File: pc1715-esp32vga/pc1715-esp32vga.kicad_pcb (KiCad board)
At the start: 2 copper layers, 110 x 38 mm, 31 parts, among them J1001 IDC10_VIDEO_IN, J1002 VGAOUT, J1003 USB_B, J1004 KEYPAD, J1005 IDC16_VGAOUT, SW1001 RST, U1001 ESP32-S3-WROOM-1, U1002 LM1117MP-3.3

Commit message: IDC10 Beschriftung
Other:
- board text added: "10 8 6 4 2"
- board text added: "10 BSYNC 6 INTENS 4 VIDEO 1,2 +5V 3 +3,3V 5,7,8,9 GND"
- board text added: "9 7 5 3 1"
- board text removed: "10 BSYNC 6 INTENS 4 VIDEO 1,2 +5V 3,5,7,8,9 GND"
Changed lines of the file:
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@@
 		(layer "Edge.Cuts")
+	)
+	(gr_text "10 8 6 4 2"
+		(at 162.56 76.708 0)
+		(layer "B.SilkS")
+		(effects
+			(font
+				(size 1.25 1.25)
+				(thickness 0.25)
+				(bold yes)
+			)
+			(justify left bottom mirror)
+		)
+	)
+	(gr_text "9 7  5  3 1"
+		(at 162.56 84.582 0)
+		(layer "B.SilkS")
+		(effects
+			(font
+				(size 1.25 1.25)
+				(thickness 0.25)
+				(bold yes)
+			)
+			(justify left bottom mirror)
+		)
 	)
 	(gr_text "Robotron VGA Adapter\nDesign (c)2024 M. Goegel\nRev 1"
@@
 		)
 	)
-	(gr_text "10 BSYNC\n6  INTENS\n4  VIDEO\n1,2 +5V\n3,5,7,8,9 GND"
+	(gr_text "10 BSYNC\n6  INTENS\n4  VIDEO\n1,2 +5V\n3	+3,3V\n5,7,8,9 GND"
 		(at 142.494 74.93 0)
 		(layer "F.SilkS")

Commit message: Prototype #1 Gerber files added
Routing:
- net GND: track 41.3 -> 43.0 mm, vias 24 -> 23
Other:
- board size 110 x 38 mm -> 112 x 38 mm
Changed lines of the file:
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@@
 			(outputformat 1)
 			(mirror no)
-			(drillshape 1)
+			(drillshape 0)
 			(scaleselection 1)
-			(outputdirectory "")
+			(outputdirectory "gerber")
 		)
 	)
@@
 			(size 1.425 1.75)
 			(layers "F.Cu" "F.Paste" "F.Mask")
-			(roundrect_rratio 0.175439)
+			(roundrect_rratio 0.1754392982)
 			(net 16 "Net-(D1003-K)")
 			(pinfunction "K")
@@
 			(size 1.425 1.75)
 			(layers "F.Cu" "F.Paste" "F.Mask")
-			(roundrect_rratio 0.175439)
+			(roundrect_rratio 0.1754392982)
 			(net 8 "+3.3V")
 			(pinfunction "A")
@@
 			(size 1.5 2.35)
 			(layers "F.Cu" "F.Paste" "F.Mask")
-			(roundrect_rratio 0.166667)
+			(roundrect_rratio 0.1666673333)
 			(net 9 "+5V")
 			(pintype "passive")
@@
 			(size 1.5 2.35)
 			(layers "F.Cu" "F.Paste" "F.Mask")
-			(roundrect_rratio 0.166667)
+			(roundrect_rratio 0.1666673333)
 			(net 7 "GND")
 			(pintype "passive")
@@
 			(size 1.2 1.4)
 			(layers "F.Cu" "F.Paste" "F.Mask")
-			(roundrect_rratio 0.208333)
+			(roundrect_rratio 0.2083333333)
 			(net 53 "Net-(U1001-EN)")
 			(pintype "passive")
@@
 			(size 1.2 1.4)
 			(layers "F.Cu" "F.Paste" "F.Mask")
-			(roundrect_rratio 0.208333)
+			(roundrect_rratio 0.2083333333)
 			(net 8 "+3.3V")
 			(pintype "passive")
@@
 			(size 1.2 1.4)
 			(layers "F.Cu" "F.Paste" "F.Mask")
-			(roundrect_rratio 0.208333)
+			(roundrect_rratio 0.2083333333)
 			(net 23 "/R1")
 			(pintype "passive")
@@
 			(size 1.2 1.4)
 			(layers "F.Cu" "F.Paste" "F.Mask")
-			(roundrect_rratio 0.208333)
+			(roundrect_rratio 0.2083333333)
 			(net 3 "/RED")
 			(pintype "passive")
@@
 			(layers "*.Cu" "*.Mask")
 			(remove_unused_layers no)
-			(roundrect_rratio 0.147059)
+			(roundrect_rratio 0.1470588235)
 			(net 1 "Net-(D1001-A)")
 			(pinfunction "Pin_1")
@@
 			(size 1.2 1.4)
 			(layers "F.Cu" "F.Paste" "F.Mask")
-			(roundrect_rratio 0.208333)
+			(roundrect_rratio 0.2083333333)
 			(net 8 "+3.3V")
 			(pintype "passive")
@@
 			(size 1.2 1.4)
 			(layers "F.Cu" "F.Paste" "F.Mask")
-			(roundrect_rratio 0.208333)
+			(roundrect_rratio 0.2083333333)
 			(net 43 "/BSYNC")
 			(pintype "passive")
@@
 			(size 1.2 1.4)
 			(layers "F.Cu" "F.Paste" "F.Mask")
-			(roundrect_rratio 0.208333)
+			(roundrect_rratio 0.2083333333)
 			(net 7 "GND")
 			(pintype "passive")
@@
 			(size 1.2 1.4)
 			(layers "F.Cu" "F.Paste" "F.Mask")
-			(roundrect_rratio 0.208333)
+			(roundrect_rratio 0.2083333333)
 			(net 16 "Net-(D1003-K)")
 			(pintype "passive")
@@
 			(size 1.2 1.4)
 			(layers "F.Cu" "F.Paste" "F.Mask")
-			(roundrect_rratio 0.208333)
+			(roundrect_rratio 0.2083333333)
 			(net 21 "/G1")
 			(pintype "passive")
@@
 			(size 1.2 1.4)
 			(layers "F.Cu" "F.Paste" "F.Mask")
-			(roundrect_rratio 0.208333)
+			(roundrect_rratio 0.2083333333)
 			(net 4 "/GREEN")
 			(pintype "passive")
@@
 		(tags "Through hole vertical IDC box header THT 2x08 2.54mm double row")
 		(property "Reference" "J1005"
-			(at 2.808 -4.048 -90)
+			(at 4.04 -6.38 -90)
 			(layer "F.SilkS")
 			(effects
@@
 			(layers "*.Cu" "*.Mask")
 			(remove_unused_layers no)
-			(roundrect_rratio 0.147059)
+			(roundrect_rratio 0.1470588235)
 			(net 3 "/RED")
 			(pinfunction "Pin_1")
@@
 			(size 1.2 1.4)
 			(layers "F.Cu" "F.Paste" "F.Mask")
-			(roundrect_rratio 0.208333)
+			(roundrect_rratio 0.2083333333)
 			(net 19 "/B1")
 			(pintype "passive")
@@
 			(size 1.2 1.4)
 			(layers "F.Cu" "F.Paste" "F.Mask")
-			(roundrect_rratio 0.208333)
+			(roundrect_rratio 0.2083333333)
 			(net 5 "/BLUE")
 			(pintype "passive")
@@
 			(size 1.2 1.4)
 			(layers "F.Cu" "F.Paste" "F.Mask")
-			(roundrect_rratio 0.208333)
+			(roundrect_rratio 0.2083333333)
 			(net 8 "+3.3V")
 			(pintype "passive")
@@
 			(size 1.2 1.4)
 			(layers "F.Cu" "F.Paste" "F.Mask")
-			(roundrect_rratio 0.208333)
+			(roundrect_rratio 0.2083333333)
 			(net 42 "/INTENS")
 			(pintype "passive")
@@
 			(size 1.2 1.4)
 			(layers "F.Cu" "F.Paste" "F.Mask")
-			(roundrect_rratio 0.208333)
+			(roundrect_rratio 0.2083333333)
 			(net 8 "+3.3V")
 			(pintype "passive")
@@
 			(size 1.2 1.4)
 			(layers "F.Cu" "F.Paste" "F.Mask")
-			(roundrect_rratio 0.208333)
+			(roundrect_rratio 0.2083333333)
 			(net 40 "/VIDEO")
 			(pintype "passive")
@@
 			(size 1.5 2.35)
 			(layers "F.Cu" "F.Paste" "F.Mask")
-			(roundrect_rratio 0.166667)
+			(roundrect_rratio 0.1666673333)
 			(net 8 "+3.3V")
 			(pintype "passive")
@@
 			(size 1.5 2.35)
 			(layers "F.Cu" "F.Paste" "F.Mask")
-			(roundrect_rratio 0.166667)
+			(roundrect_rratio 0.1666673333)
 			(net 7 "GND")
 			(pintype "passive")
@@
 			(size 1.2 1.4)
 			(layers "B.Cu" "B.Paste" "B.Mask")
-			(roundrect_rratio 0.208333)
+			(roundrect_rratio 0.2083333333)
 			(net 22 "/G2")
 			(pintype "passive")
@@
 			(size 1.2 1.4)
 			(layers "B.Cu" "B.Paste" "B.Mask")
-			(roundrect_rratio 0.208333)
+			(roundrect_rratio 0.2083333333)
 			(net 4 "/GREEN")
 			(pintype "passive")
@@
 			(size 1.2 1.4)
 			(layers "B.Cu" "B.Paste" "B.Mask")
-			(roundrect_rratio 0.208333)
+			(roundrect_rratio 0.2083333333)
 			(net 20 "/B2")
 			(pintype "passive")
@@
 			(size 1.2 1.4)
 			(layers "B.Cu" "B.Paste" "B.Mask")
-			(roundrect_rratio 0.208333)
+			(roundrect_rratio 0.2083333333)
 			(net 5 "/BLUE")
 			(pintype "passive")
@@
 			(size 1.2 1.4)
 			(layers "B.Cu" "B.Paste" "B.Mask")
-			(roundrect_rratio 0.208333)
+			(roundrect_rratio 0.2083333333)
 			(net 24 "/R2")
 			(pintype "passive")
@@
 			(size 1.2 1.4)
 			(layers "B.Cu" "B.Paste" "B.Mask")
-			(roundrect_rratio 0.208333)
+			(roundrect_rratio 0.2083333333)
 			(net 3 "/RED")
 			(pintype "passive")
@@
 	)
 	(gr_rect
-		(start 106 49)
+		(start 104 49)
 		(end 216 87)
 		(stroke
@@
 		)
 	)
+	(dimension
+		(type aligned)
+		(layer "User.9")
+		(pts
+			(xy 110 80) (xy 104 80)
+		)
+		(height -15)
+		(gr_text "6,0000 mm"
+			(at 107 93.2 0)
+			(layer "User.9")
+			(effects
+				(font
+					(size 1.5 1.5)
+					(thickness 0.3)
+				)
+			)
+		)
+		(format
+			(prefix "")
+			(suffix "")
+			(units 3)
+			(units_format 1)
+			(precision 4)
+		)
+		(style
+			(thickness 0.2)
+			(arrow_length 1.27)
+			(text_position_mode 0)
+			(extension_height 0.58642)
+			(extension_offset 0.5) keep_text_aligned)
+	)
+	(dimension
+		(type aligned)
+		(layer "User.9")
+		(pts
+			(xy 210 80) (xy 216 80)
+		)
+		(height 12.5)
+		(gr_text "6,0000 mm"
+			(at 213 90.7 0)
+			(layer "User.9")
+			(effects
+				(font
+					(size 1.5 1.5)
+					(thickness 0.3)
+				)
+			)
+		)
+		(format
+			(prefix "")
+			(suffix "")
+			(units 3)
+			(units_format 1)
+			(precision 4)
+		)
+		(style
+			(thickness 0.2)
+			(arrow_length 1.27)
+			(text_position_mode 0)
+			(extension_height 0.58642)
+			(extension_offset 0.5) keep_text_aligned)
+	)
 	(segment
 		(start 151.6725 81)
@@
 	)
 	(via
-		(at 152.908 79.502)
-		(size 0.8)
-		(drill 0.4)
-		(layers "F.Cu" "B.Cu")
-		(free yes)
-		(net 7)
-	)
-	(via
 		(at 188.468 64.516)
 		(size 0.8)
@@
 	)
 	(segment
+		(start 155.5 79.25)
+		(end 155.5 77.5)
+		(width 0.25)
+		(layer "B.Cu")
+		(net 7)
+	)
+	(segment
 		(start 130.3225 59.2825)
 		(end 132.4475 59.2825)
@@
 		(polygon
 			(pts
-				(xy 106.426 49.53) (xy 215.392 49.53) (xy 215.646 49.784) (xy 215.646 86.614) (xy 106.426 86.614)
+				(xy 104.426 49.53) (xy 215.392 49.53) (xy 215.646 49.784) (xy 215.646 86.614) (xy 104.426 86.614)
 			)
 		)
@@
 		(polygon
 			(pts
-				(xy 106.5 49.5) (xy 215.5 49.5) (xy 215.5 86.5) (xy 106.5 86.5)
+				(xy 104.5 49.5) (xy 215.5 49.5) (xy 215.5 86.5) (xy 104.5 86.5)
 			)
 		)

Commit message: Revision 2
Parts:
- removed D1001, D1002: 1N5819, Diode_THT:D_DO-41_SOD81_P7.62mm_Horizontal
- removed D1003: LED, LED_SMD:LED_1206_3216Metric_Pad1.42x1.75mm_HandSolder
- removed R1001: 300, Resistor_SMD:R_0805_2012Metric_Pad1.20x1.40mm_HandSolder
- removed R1002, R1003, R1011: 330, Resistor_SMD:R_0805_2012Metric_Pad1.20x1.40mm_HandSolder
- removed TP1001: TP_SPI, TestPoint:TestPoint_Pad_1.5x1.5mm
- removed TP1002: TP_COPY, TestPoint:TestPoint_Pad_1.5x1.5mm
- added D1: BAT54C Uf 0,24V, Package_TO_SOT_SMD:SOT-23, B.Cu at (105.9, 115.5)
- added D2: 3V3, LED_SMD:LED_1206_3216Metric_Pad1.42x1.75mm_HandSolder, F.Cu at (129.3, 128.6)
- added D3: SYNC, LED_SMD:LED_1206_3216Metric_Pad1.42x1.75mm_HandSolder, F.Cu at (129.3, 133.7)
- added D4: STAT, LED_SMD:LED_1206_3216Metric_Pad1.42x1.75mm_HandSolder, F.Cu at (129.3, 131.2)
- added J6: USB_C_Receptacle_USB2.0_16P, Connector_USB:USB_C_Receptacle_GCT_USB4105-xx-A_16P_TopMnt_Horizontal, F.Cu at (112.5, 103.6)
- added J7: DBG, Connector_PinHeader_2.54mm:PinHeader_1x07_P2.54mm_Vertical, F.Cu at (160.3, 134.1)
- added R11: 330, Resistor_SMD:R_0805_2012Metric_Pad1.20x1.40mm_HandSolder, B.Cu at (112.0, 123.9)
- added R12: 330, Resistor_SMD:R_0805_2012Metric_Pad1.20x1.40mm_HandSolder, B.Cu at (114.1, 123.9)
- added R13: 330, Resistor_SMD:R_0805_2012Metric_Pad1.20x1.40mm_HandSolder, B.Cu at (116.3, 123.9)
- added R2: 330, Resistor_SMD:R_0805_2012Metric_Pad1.20x1.40mm_HandSolder, B.Cu at (128.8, 128.6)
- added R3: 330, Resistor_SMD:R_0805_2012Metric_Pad1.20x1.40mm_HandSolder, B.Cu at (128.8, 133.7)
- added R4: 330, Resistor_SMD:R_0805_2012Metric_Pad1.20x1.40mm_HandSolder, B.Cu at (128.8, 131.2)
- J4: renamed from J1004; footprint Connector_PinHeader_2.54mm:PinHeader_1x05_P2.54mm_Vertical -> Connector_PinSocket_2.54mm:PinSocket_1x05_P2.54mm_Horizontal; moved to B.Cu
- JP1: renamed from JP1001; footprint Connector_PinSocket_2.54mm:PinSocket_1x02_P2.54mm_Vertical -> Connector_PinHeader_2.54mm:PinHeader_1x02_P2.54mm_Vertical
- R1: renamed from R1010; moved to B.Cu
- R5: renamed from R1004; moved to B.Cu
- R7: renamed from R1006; moved to B.Cu
- R9: renamed from R1008; moved to B.Cu
- moved R1 73.9 mm to (137.4, 130.8), turned to 180 degrees
- moved SW1 71.5 mm to (138.7, 130.8)
- moved C1 67.4 mm to (127.2, 109.9)
- moved C2 67.4 mm to (123.7, 109.9)
- moved H1001 67.4 mm to (66.0, 106.0)
- moved H1002 67.4 mm to (66.0, 131.0)
- moved H1003 67.4 mm to (166.0, 106.0)
- moved H1004 67.4 mm to (166.0, 131.0)
- moved J1 67.4 mm to (107.7, 132.0)
- moved J2 67.4 mm to (86.0, 111.5)
- moved J3 67.4 mm to (111.2, 115.4)
- moved R10 67.4 mm to (135.1, 112.6)
- moved R6 67.4 mm to (135.1, 105.6)
- moved R8 67.4 mm to (135.1, 109.1)
- moved U1 67.4 mm to (126.7, 108.4)
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- renumbered C1001 to C1, C1002 to C2, J1001 to J1, J1002 to J2, J1003 to J3, J1005 to J5, R1009 to R10, R1005 to R6, R1007 to R8, SW1001 to SW1, U1002 to U1, U1001 to U2
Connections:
- net Net-(D1001-A) renamed /5V_VID
- J3 pad 1: Net-(D1002-A) -> /VBUS
- J4 pad 1: /K_LEFT -> /K_RIGHT
- J4 pad 2: /K_UP -> /K_DOWN
- J4 pad 4: /K_DOWN -> /K_UP
- J4 pad 5: /K_RIGHT -> /K_LEFT
- U2 pad 16: unconnected-(U1001-GPIO46-Pad16) -> Net-(D3-A)
- U2 pad 19: unconnected-(U1001-GPIO11/TOUCH11/ADC2_CH0/FSPID/FSPIIO5/SUBSPID-Pad19) -> /TP_11
- U2 pad 20: unconnected-(U1001-GPIO12/TOUCH12/ADC2_CH1/FSPICLK/FSPIIO6/SUBSPICLK-Pad20) -> /TP_12
- U2 pad 21: Net-(U1001-GPIO13/TOUCH13/ADC2_CH2/FSPIQ/FSPIIO7/SUBSPIQ) -> /TP_SPI
- U2 pad 22: Net-(U1001-GPIO14/TOUCH14/ADC2_CH3/FSPIWP/FSPIDQS/SUBSPIWP) -> /TP_CPY
- U2 pad 35: unconnected-(U1001-MTMS/GPIO42-Pad35) -> Net-(D4-A)
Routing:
- net Net-(D4-A): track 0.00 -> 47.9 mm, vias 0 -> 2
- net /TP_SPI: track 0.00 -> 31.5 mm, vias 0 -> 2
- net /TP_11: track 0.00 -> 30.3 mm, vias 0 -> 1
- net Net-(D3-A): track 0.00 -> 30.1 mm, vias 0 -> 2
- net /TP_CPY: track 0.00 -> 25.9 mm, vias 0 -> 2
- net Net-(U1001-GPIO14/TOUCH14/ADC2_CH3/FSPIWP/FSPIDQS/SUBSPIWP): track 25.0 -> 0.00 mm, vias 2 -> 0
- net /TP_12: track 0.00 -> 23.0 mm, vias 0 -> 1
- net Net-(U1001-GPIO13/TOUCH13/ADC2_CH2/FSPIQ/FSPIIO7/SUBSPIQ): track 22.0 -> 0.00 mm, vias 2 -> 0
- net /VBUS: track 0.00 -> 21.7 mm, vias 0 -> 1
- net /INTENS: track 52.6 -> 68.7 mm
- net /BSYNC: track 51.6 -> 65.5 mm, vias 2 -> 4
- net Net-(JP1-A): track 7.44 -> 19.3 mm, vias 0 -> 1
- net /USB_DN: track 27.2 -> 39.0 mm, vias 0 -> 1
- net /VIDEO: track 58.7 -> 69.8 mm, vias 2 -> 3
- net /GREEN: track 83.6 -> 94.6 mm
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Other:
- board text added: "BS"
- board text added: "INT"
- board text added: "J3"
- board text added: "Robotron VGA Adapter Design (c)2024 M. Goegel Rev 2"
- board text added: "TP11"
- board text added: "TP12"
- board text added: "TP_CPY"
- board text added: "TP_SPI"
- board text added: "VID"
- board text removed: "Robotron VGA Adapter Design (c)2024 M. Goegel Rev 1"

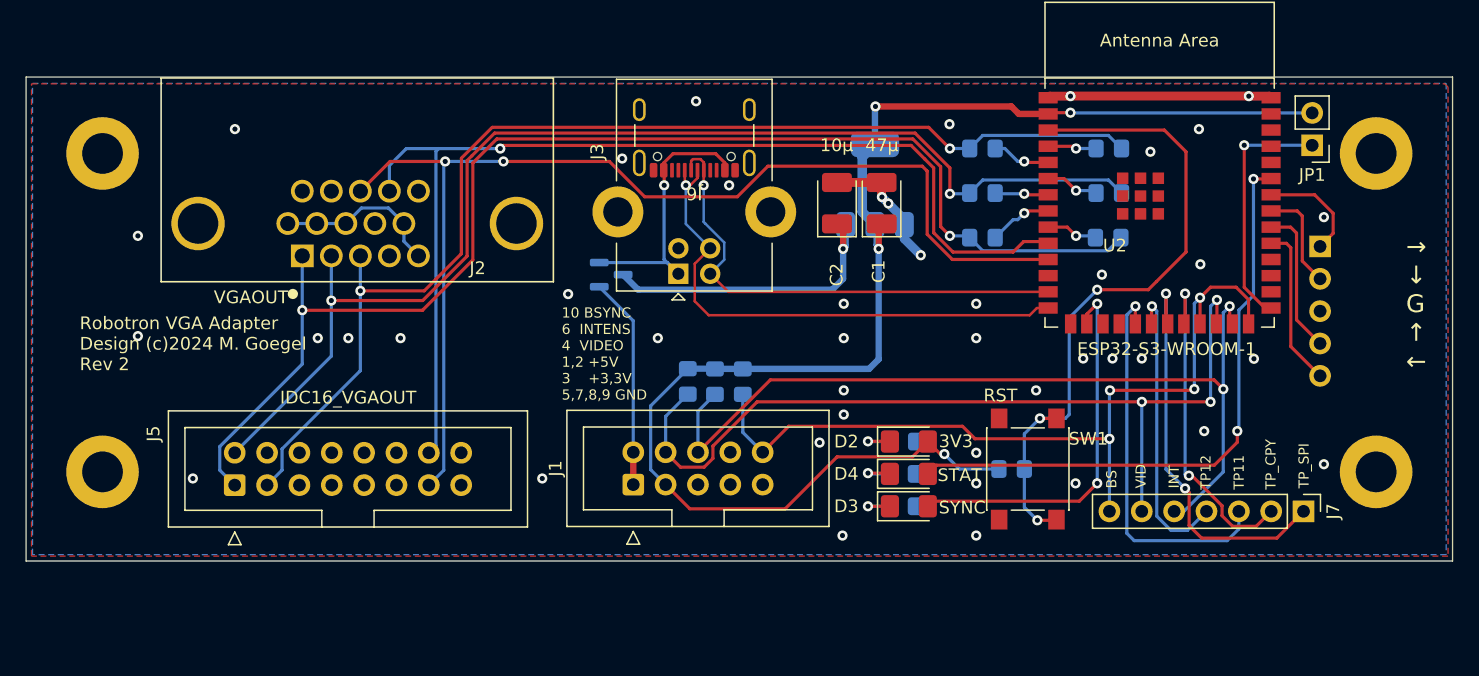
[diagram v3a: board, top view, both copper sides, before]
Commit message: Rev 2 Main PCB with keypad
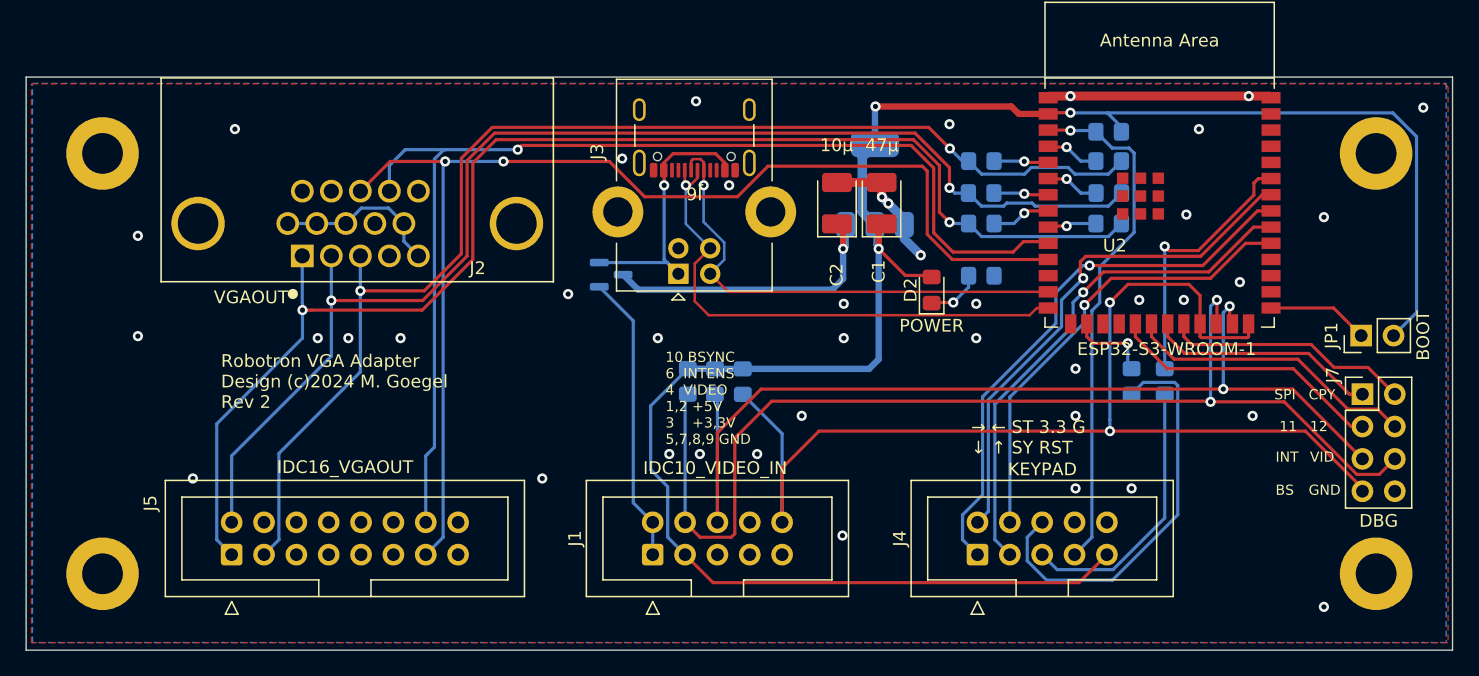
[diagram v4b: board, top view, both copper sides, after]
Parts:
- removed D3: SYNC, LED_SMD:LED_1206_3216Metric_Pad1.42x1.75mm_HandSolder
- removed D4: STAT, LED_SMD:LED_1206_3216Metric_Pad1.42x1.75mm_HandSolder
- removed SW1: RST, Button_Switch_SMD:SW_Push_1P1T_NO_6x6mm_H9.5mm
- D2: value 3V3 -> POWER; footprint LED_SMD:LED_1206_3216Metric_Pad1.42x1.75mm_HandSolder -> Diode_SMD:D_0805_2012Metric_Pad1.15x1.40mm_HandSolder
- J4: footprint Connector_PinSocket_2.54mm:PinSocket_1x05_P2.54mm_Horizontal -> Connector_IDC:IDC-Header_2x05_P2.54mm_Vertical; moved to F.Cu
- J7: footprint Connector_PinHeader_2.54mm:PinHeader_1x07_P2.54mm_Vertical -> Connector_PinHeader_2.54mm:PinHeader_2x04_P2.54mm_Vertical
- moved J4 36.2 mm to (134.7, 137.5), turned to 90 degrees
- moved R1 27.5 mm to (145.0, 104.3), turned to 0 degrees
- moved R4 21.8 mm to (149.4, 123.9), turned to 90 degrees
- moved R3 20.5 mm to (146.8, 123.9), turned to 90 degrees
- moved JP1 15.4 mm to (164.8, 120.3), turned to 90 degrees
- moved R2 14.4 mm to (135.0, 115.6)
- moved D2 12.0 mm to (131.1, 116.7), turned to 90 degrees
- moved J7 10.3 mm to (164.9, 124.9), turned to 0 degrees
- moved H1002 8.00 mm to (66.0, 139.0)
- moved H1004 8.00 mm to (166.0, 139.0)
- moved J1 5.71 mm to (109.2, 137.5)
- moved J5 5.47 mm to (76.1, 137.5)
- moved R10 1.11 mm to (135.0, 111.5)
- moved R9 1.11 mm to (145.0, 111.5)
- moved R6 0.99 mm to (135.0, 106.6)
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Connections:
- J4 pad 1: /K_RIGHT -> /K_DOWN
- J4 pad 2: /K_DOWN -> /K_RIGHT
- J4 pad 3: GND -> /K_UP
- J4 pad 4: /K_UP -> /K_LEFT
- J4 pad 5: /K_LEFT -> /L_STAT
- R1 pad 1: Net-(U2-EN) -> /RST
- R3 pad 1: GND -> /L_SYNC
- R3 pad 2: Net-(D3-K) -> Net-(U2-GPIO46)
- R4 pad 1: GND -> /L_STAT
- R4 pad 2: Net-(D4-K) -> Net-(U2-MTMS/GPIO42)
- U2 pad 16: Net-(D3-A) -> Net-(U2-GPIO46)
- U2 pad 3: Net-(U2-EN) -> /RST
- U2 pad 35: Net-(D4-A) -> Net-(U2-MTMS/GPIO42)
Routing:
- net Net-(U2-EN): track 52.5 -> 0.00 mm, vias 3 -> 0
- net Net-(D4-A): track 47.9 -> 0.00 mm, vias 2 -> 0
- net +3.3V: track 113.7 -> 157.0 mm, vias 4 -> 3
- net /RST: track 0.00 -> 41.0 mm, vias 0 -> 1
- net /K_DOWN: track 8.13 -> 43.7 mm, vias 0 -> 1
- net /K_RIGHT: track 8.50 -> 41.1 mm, vias 0 -> 1
- net /L_SYNC: track 0.00 -> 32.3 mm
- net Net-(D3-A): track 30.1 -> 0.00 mm, vias 2 -> 0
- net /K_UP: track 11.6 -> 40.9 mm, vias 0 -> 1
- net /BSYNC: track 65.5 -> 90.6 mm, vias 4 -> 2
- net /K_LEFT: track 12.7 -> 36.1 mm, vias 0 -> 1
- net /L_STAT: track 0.00 -> 21.5 mm
- net Net-(U2-MTMS/GPIO42): track 0.00 -> 21.0 mm, vias 0 -> 1
- net /VIDEO: track 69.8 -> 88.0 mm, vias 3 -> 2
- net /TP_SPI: track 31.5 -> 18.4 mm, vias 2 -> 0
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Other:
- board size 112 x 38 mm -> 112 x 45 mm
- board text added: "11"
- board text added: "12"
- board text added: "CPY"
- board text added: "GND"
- board text added: "SPI"
- board text added: "→ ← ST 3.3 G ↓ ↑ SY RST"
- board text removed: "TP11"
- board text removed: "TP12"
- board text removed: "TP_CPY"
- board text removed: "TP_SPI"
- board text removed: "→ ↓ G ↑ ←"

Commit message: Documentation improved
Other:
- board text added: "JLCJLCJLCJLC"
- board text added: "K"
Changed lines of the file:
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@@
+		)
+	)
+	(gr_text "K"
+		(at 133.4 118.9 90)
+		(layer "F.SilkS")
+		(effects
+			(font
+				(size 1 1)
+				(thickness 0.1)
+			)
+			(justify left bottom)
 		)
 	)
@@
 		(layer "F.SilkS")
 		(effects
+			(font
+				(size 1 1)
+				(thickness 0.15)
+			)
+			(justify left bottom)
+		)
+	)
+	(gr_text "JLCJLCJLCJLC"
+		(at 143.55 102.1 0)
+		(layer "F.SilkS")
+		(effects
